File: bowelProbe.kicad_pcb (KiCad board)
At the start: 2 copper layers, 169.5 x 83.2 mm, 93 parts, among them J1 Conn_01x01, J10 Conn_01x01, J11 Conn_01x01, J12 Conn_01x01, J13 Conn_01x01, J14 Conn_01x01, J15 Conn_01x01, J16 Conn_01x01, J17 Conn_01x01, J18 Conn_01x01, J19 Conn_01x01, J2 Conn_01x01, J20 Conn_01x01, J3 Conn_01x01, J4 Conn_01x01, J5 Conn_02x03_Odd_Even, J6 Conn_01x08, J7 Conn_01x01, J8 Conn_01x01, J9 Conn_01x01, U1 L7805CV, U2 LT8330, U3 ATmega328P, U4 AD9833BRMZ, U5 Buffer, U6 OPA2134UA/2K5, U7 TL072ACDR, U8 MCP6002-E/MC

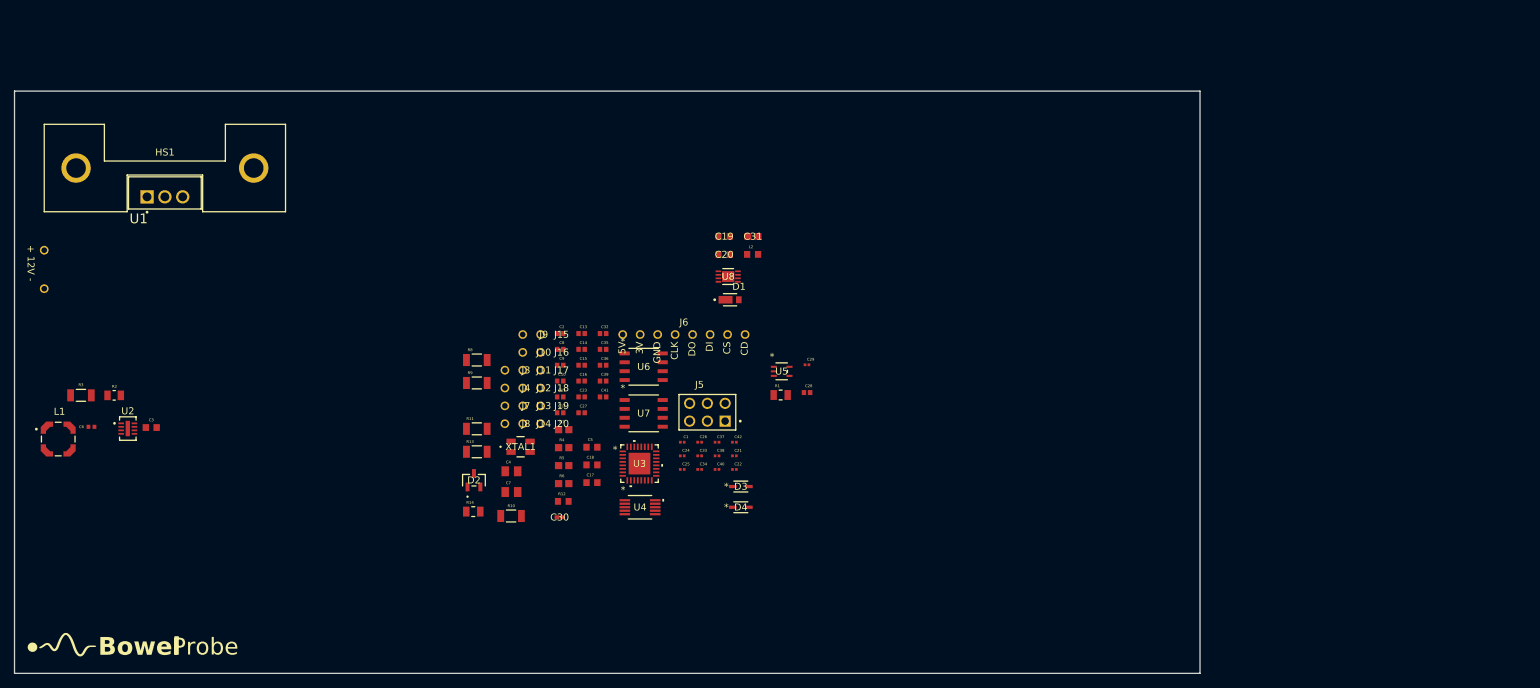
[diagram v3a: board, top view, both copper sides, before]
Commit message: PCB Layout Progress
Initial rough layout of parts into corresponding sections. Next up is to formalize signal, power, and SPI flow as well as specific component placements.
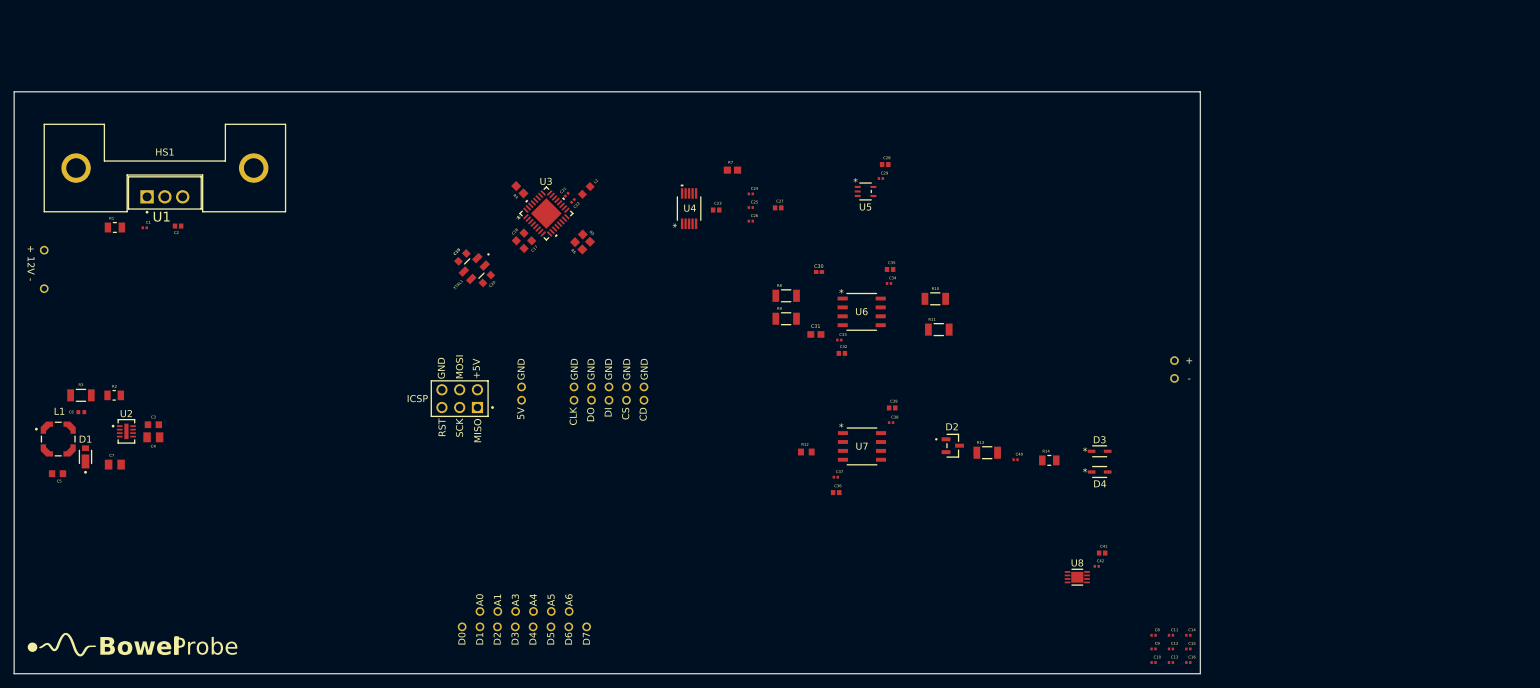
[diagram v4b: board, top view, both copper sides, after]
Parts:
- added J21: Conn_01x08, BowelProbe:microSD, F.Cu at (142.5, 87.8)
- C10, C11, C12, C13, C14, C15, C16, C8, C9: value 10u -> 0.1u; footprint BowelProbe:Cap10uF -> BowelProbe:Cap0.1uF
- moved R1 98.2 mm to (75.6, 65.0)
- moved C13 96.5 mm to (226.6, 127.2)
- moved C14 95.9 mm to (229.1, 123.3)
- moved C15 95.8 mm to (229.1, 125.3)
- moved + 95.7 mm to (227.1, 84.0)
- moved - 95.7 mm to (227.1, 86.6)
- moved C16 95.6 mm to (229.1, 127.2)
- moved D1 94.9 mm to (71.4, 97.8), turned to 90 degrees
- moved C8 94.2 mm to (224.1, 123.3)
- moved C9 94.0 mm to (224.1, 125.3)
- moved C10 93.9 mm to (224.1, 127.2)
- moved C11 93.7 mm to (226.6, 123.3)
- moved C12 93.6 mm to (226.6, 125.3)
- moved C1 82.7 mm to (79.9, 65.0)
- moved R14 82.7 mm to (209.2, 98.3)
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- renumbered J3 to +, J4 to -, J15 to A0, J16 to A1, J17 to A3, J18 to A4, J19 to A5, J20 to A6, J7 to D0, J8 to D1, J9 to D2, J10 to D3, J11 to D4, J12 to D5, J13 to D6, J14 to D7, J5 to ICSP
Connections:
- A3 pad 1: /A2 -> /A3
- A4 pad 1: /A3 -> /A4
- A5 pad 1: /A4 -> /A5
- A6 pad 1: /A5 -> /A6
- U8 pad 1: unconnected-(U8-VOUTA-Pad1) -> Net-(U8-VINA-)
- U8 pad 2: unconnected-(U8-VINA--Pad2) -> Net-(U8-VINA-)
- U8 pad 3: unconnected-(U8-VINA+-Pad3) -> GND
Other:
- board size 169.5 x 83.2 mm -> 169.6 x 83.2 mm
- copper layers 2 -> 4
- board text added: "+5V"
- board text added: "GND"
- board text added: "MISO"
- board text added: "MOSI"
- board text added: "RST"
- board text added: "SCK"

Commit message: Schematic and Layout Updates
Added 47 ohm resistors to schematic to reduce ringing of SPI through ports and added corresponding info to BOM. Set PCB layout. May make a few more small tweaks.
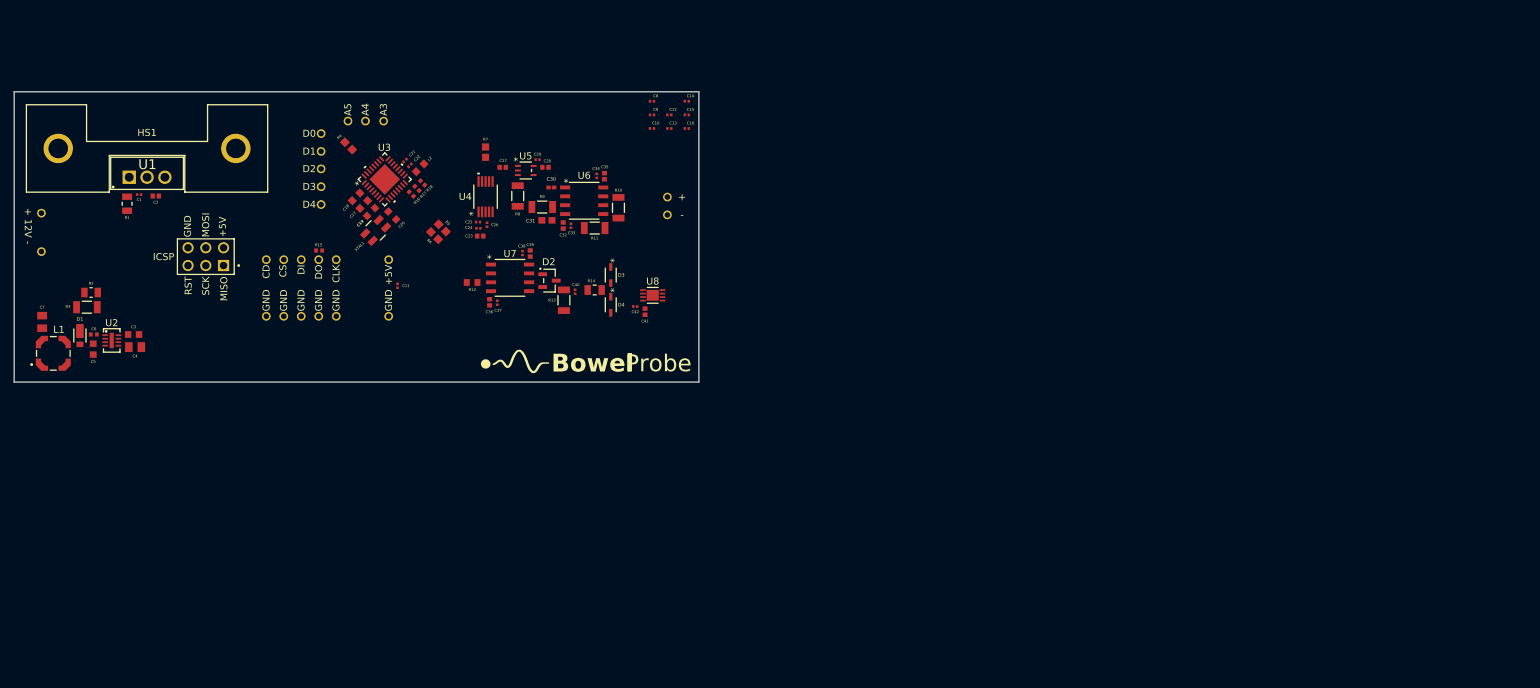
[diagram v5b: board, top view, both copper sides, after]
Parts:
- removed A0, A1, A6, D5, D6, D7: Conn_01x01, BowelProbe:CT3149-0
- added R15: 47, BowelProbe:Resistor47, F.Cu at (104.8, 68.3)
- added R16: 47, BowelProbe:Resistor47, F.Cu at (118.0, 60.2)
- added R17: 47, BowelProbe:Resistor47, F.Cu at (118.8, 59.4)
- added R18: 47, BowelProbe:Resistor47, F.Cu at (119.6, 58.6)
- moved C11 121.3 mm to (116.0, 73.3), turned to -90 degrees
- moved C10 104.8 mm to (152.4, 50.8)
- moved C12 104.8 mm to (154.9, 48.9)
- moved C13 104.8 mm to (154.9, 50.8)
- moved C14 104.8 mm to (157.4, 47.0)
- moved C15 104.8 mm to (157.4, 48.9)
- moved C16 104.8 mm to (157.4, 50.8)
- moved C8 104.8 mm to (152.4, 47.0)
- moved C9 104.8 mm to (152.4, 48.9)
- moved G*** 76.4 mm to (132.9, 84.7)
- moved + 76.2 mm to (154.6, 60.6)
- moved - 76.2 mm to (154.6, 63.2)
- moved A5 75.9 mm to (108.9, 49.8)
- moved C42 75.7 mm to (150.0, 76.3), turned to 180 degrees
- moved D3 74.3 mm to (146.5, 71.8), turned to -90 degrees
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- renumbered J21 to J15
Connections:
- J6 pad 5: /MISO -> Net-(J6-Pin_5)
- U3 pad 15: /MOSI -> Net-(U3-PB3)
- U3 pad 16: /MISO -> Net-(U3-PB4)
- U3 pad 17: /SCK -> Net-(U3-PB5)
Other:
- board size 169.6 x 83.2 mm -> 97.9 x 41.5 mm

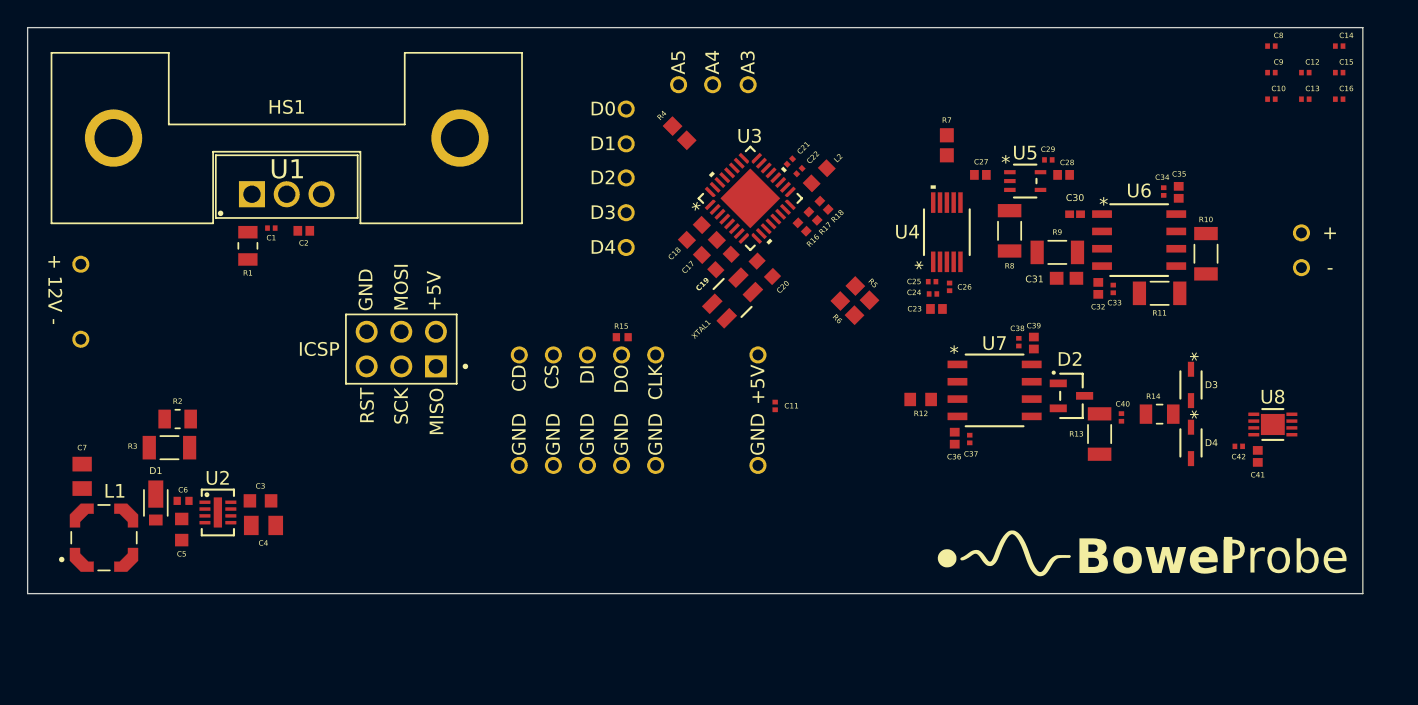
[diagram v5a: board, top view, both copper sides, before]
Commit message: PCB Layout Plan Finalized
Added more stitching capacitors in schematic. Decided on final layout and added necessary vias. Added NPTH M3 mounting holes.
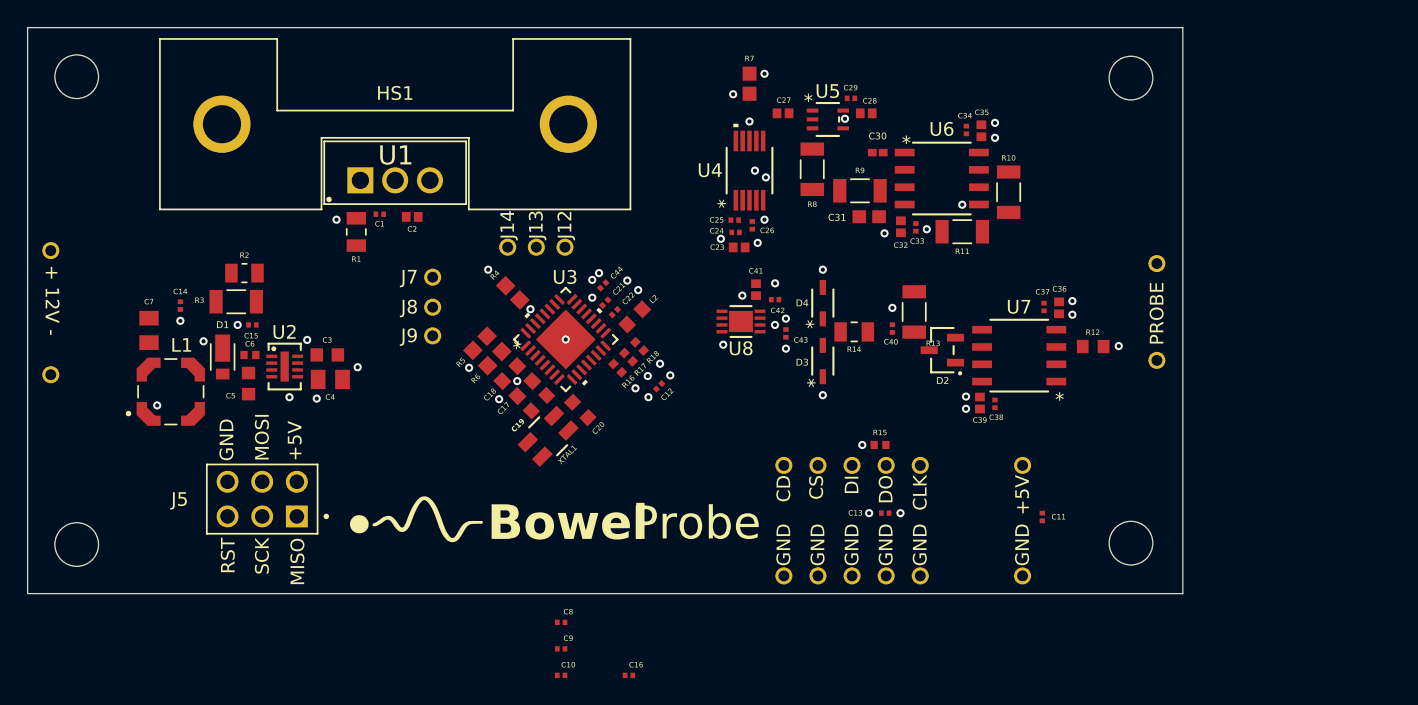
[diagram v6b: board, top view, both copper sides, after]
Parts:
- removed the D3 at (105.1, 59.2)
- removed the D4 at (105.1, 61.7)
- added C43: 0.1u, BowelProbe:Cap0.1uF, F.Cu at (116.8, 68.0)
- added C44: 0.1u, BowelProbe:Cap0.1uF, F.Cu at (103.4, 64.5)
- added REF**: MountingHole_3.2mm_M3, MountingHole:MountingHole_3.2mm_M3, F.Cu at (64.8, 83.5)
- added REF**: MountingHole_3.2mm_M3, MountingHole:MountingHole_3.2mm_M3, F.Cu at (142.1, 83.4)
- added REF**: MountingHole_3.2mm_M3, MountingHole:MountingHole_3.2mm_M3, F.Cu at (64.8, 49.2)
- added REF**: MountingHole_3.2mm_M3, MountingHole:MountingHole_3.2mm_M3, F.Cu at (142.1, 49.3)
- moved C14 87.1 mm to (72.4, 66.0), turned to 90 degrees
- moved C15 81.8 mm to (77.7, 67.4)
- moved C10 67.1 mm to (100.3, 93.1)
- moved C16 67.1 mm to (105.3, 93.1)
- moved C8 67.1 mm to (100.3, 89.2)
- moved C9 67.1 mm to (100.3, 91.2)
- moved C12 52.7 mm to (107.5, 71.9), turned to 45 degrees
- moved C13 43.2 mm to (124.1, 81.2)
- moved G*** 43.2 mm to (89.8, 82.2)
- moved U8 39.7 mm to (113.5, 67.2), turned to 0 degrees
- moved C41 38.8 mm to (114.6, 64.8), turned to 90 degrees
- moved C42 35.7 mm to (116.0, 65.5), turned to 0 degrees
- moved D4 28.9 mm to (119.5, 65.8), turned to 90 degrees
- moved R5 28.3 mm to (94.4, 68.7), turned to 45 degrees
- moved D3 27.1 mm to (119.5, 70.0), turned to 90 degrees
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- renumbered A3 to J12, A4 to J13, A5 to J14, + to J3, - to J4, ICSP to J5, D0 to J7, D1 to J8, D2 to J9
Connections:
- R5 pad 1: /nSS -> /+5V
- R5 pad 2: /+5V -> /CD
- R6 pad 1: /CD -> /+5V
- R6 pad 2: /+5V -> /nSS
- U3 pad 1: /D3 -> /CD
- U3 pad 13: /CD -> unconnected-(U3-PB1-Pad13)
- U3 pad 14: /nSS -> unconnected-(U3-PB2-Pad14)
- U3 pad 2: /D4 -> /nSS
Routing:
- net GND: vias 0 -> 22
- net /nSS_Sin: vias 0 -> 2
- net /nReset: vias 0 -> 1
- net /VADC: vias 0 -> 2
- net /SCK: vias 0 -> 2
- net /MOSI: vias 0 -> 2
- net /MISO: vias 0 -> 2
- net /-12V: vias 0 -> 4
- net /+5V: vias 0 -> 13
- net /+12V: vias 0 -> 6
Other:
- board size 97.9 x 41.5 mm -> 84.7 x 41.5 mm
- board text added: "PROBE"

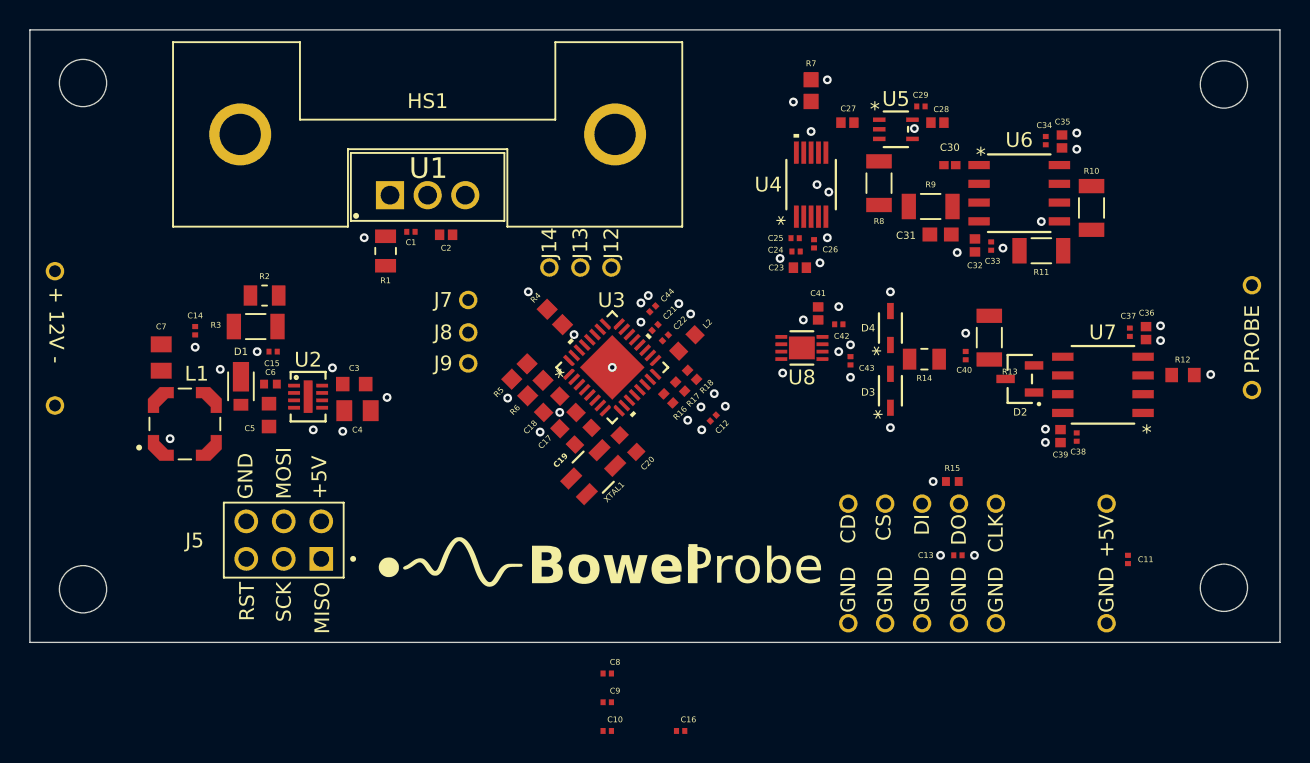
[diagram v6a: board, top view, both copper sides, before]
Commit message: PCB Layout Routed
Schematic references adjusted and extra stitching capacitors removed. Layout added a few vias and fully routed.

Layout Finalization:
- Add ground pours on L1 and L4
- Add stitching vias
- Add edge stitching vias
- Review
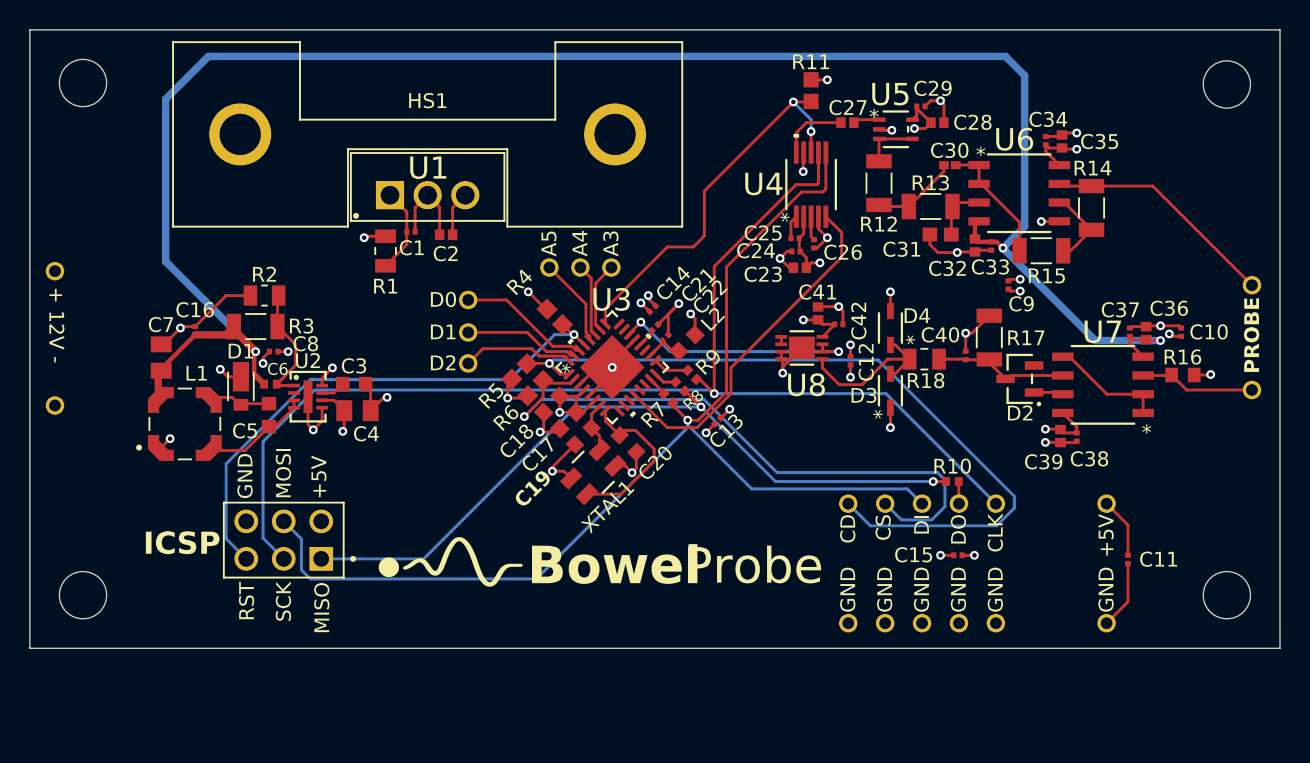
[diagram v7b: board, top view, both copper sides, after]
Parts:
- removed the C15 at (77.7, 67.4)
- removed the C16 at (105.3, 93.1)
- moved C10 47.3 mm to (139.2, 66.1), turned to 90 degrees
- moved C9 39.2 mm to (127.5, 62.9), turned to -90 degrees
- moved C8 31.4 mm to (77.7, 67.4)
- moved REF** 0.54 mm to (142.3, 83.9)
- moved REF** 0.40 mm to (64.8, 83.9)
- moved C13 0.36 mm to (107.8, 72.1)
- moved REF** 0.20 mm to (142.3, 49.3)
- renumbered J12 to A3, J13 to A4, J14 to A5, C43 to C12, C12 to C13, C44 to C14, C13 to C15, C14 to C16, J7 to D0, J8 to D1, J9 to D2, J5 to ICSP, J3 to J12, J4 to J13, J6 to J3, J15 to J4, R15 to R10, R7 to R11, R8 to R12, R9 to R13, R10 to R14, R11 to R15, R12 to R16, R13 to R17, R14 to R18, R16 to R7, R17 to R8, R18 to R9
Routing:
- net /-12V: track 0.00 -> 125.5 mm, vias 4 -> 3
- net GND: track 0.00 -> 90.3 mm, vias 22 -> 30
- net /SCK: track 0.00 -> 84.5 mm, vias 2 -> 1
- net /MOSI: track 0.00 -> 78.2 mm, vias 2 -> 1
- net /CD: track 0.00 -> 51.7 mm, vias 0 -> 1
- net /MISO: track 0.00 -> 50.2 mm
- net /nSS: track 0.00 -> 43.2 mm, vias 0 -> 1
- net /+5V: track 0.00 -> 38.7 mm
- net /nReset: track 0.00 -> 36.3 mm
- net /nSS_Sin: track 0.00 -> 26.5 mm
- net /CLKO: track 0.00 -> 23.9 mm
- net /+12V: track 0.00 -> 18.0 mm, vias 6 -> 9
- net /VADC: track 0.00 -> 17.0 mm
- net /Vamplified: track 0.00 -> 15.9 mm
- net Net-(U3-PB7): track 0.00 -> 11.4 mm
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- added copper zone on In2.Cu, net /+12V
- added copper zone on In2.Cu, net /+5V
- added copper zone on In1.Cu, net GND
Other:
- board size 84.7 x 41.5 mm -> 84.7 x 41.9 mm

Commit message: PCB Finished
Added pours and stitching to finish layout. Adjusted BOM to fit JLCPCB expected. Generated CPL file. Various KiCad plugins were downloaded. A folder "PCBA_Files" created to hold BOM, Pick and Place, and Gerber files.

Final Objectives:
- Simulate with Ansys HFSS
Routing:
- net GND: vias 30 -> 79
- added copper zone on B.Cu, net GND
- added copper zone on F.Cu, net GND
